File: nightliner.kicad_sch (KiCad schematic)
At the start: 76 parts, among them J1 TYPE-C-31-M-12, SW1 SW_SPST, SW10 SW_SPST, SW11 SW_SPST, SW12 SW_SPST, SW13 SW_SPST, SW14 SW_SPST, SW15 SW_SPST, SW16 SW_SPST, SW17 SW_SPST, SW18 SW_SPST, SW19 SW_SPST, SW2 SW_SPST, SW20 SW_SPST, SW21 ON_OFF, SW22 Reset, SW3 SW_SPST, SW4 SW_SPST, SW5 SW_SPST, SW6 SW_SPST, SW7 SW_SPST, SW8 SW_SPST, SW9 SW_SPST, U1 holyiot-18010, U2 TVS2200DRV, U3 USBLC6-2SC6, U4 BQ24075RGT, U5 XC6220B331MR

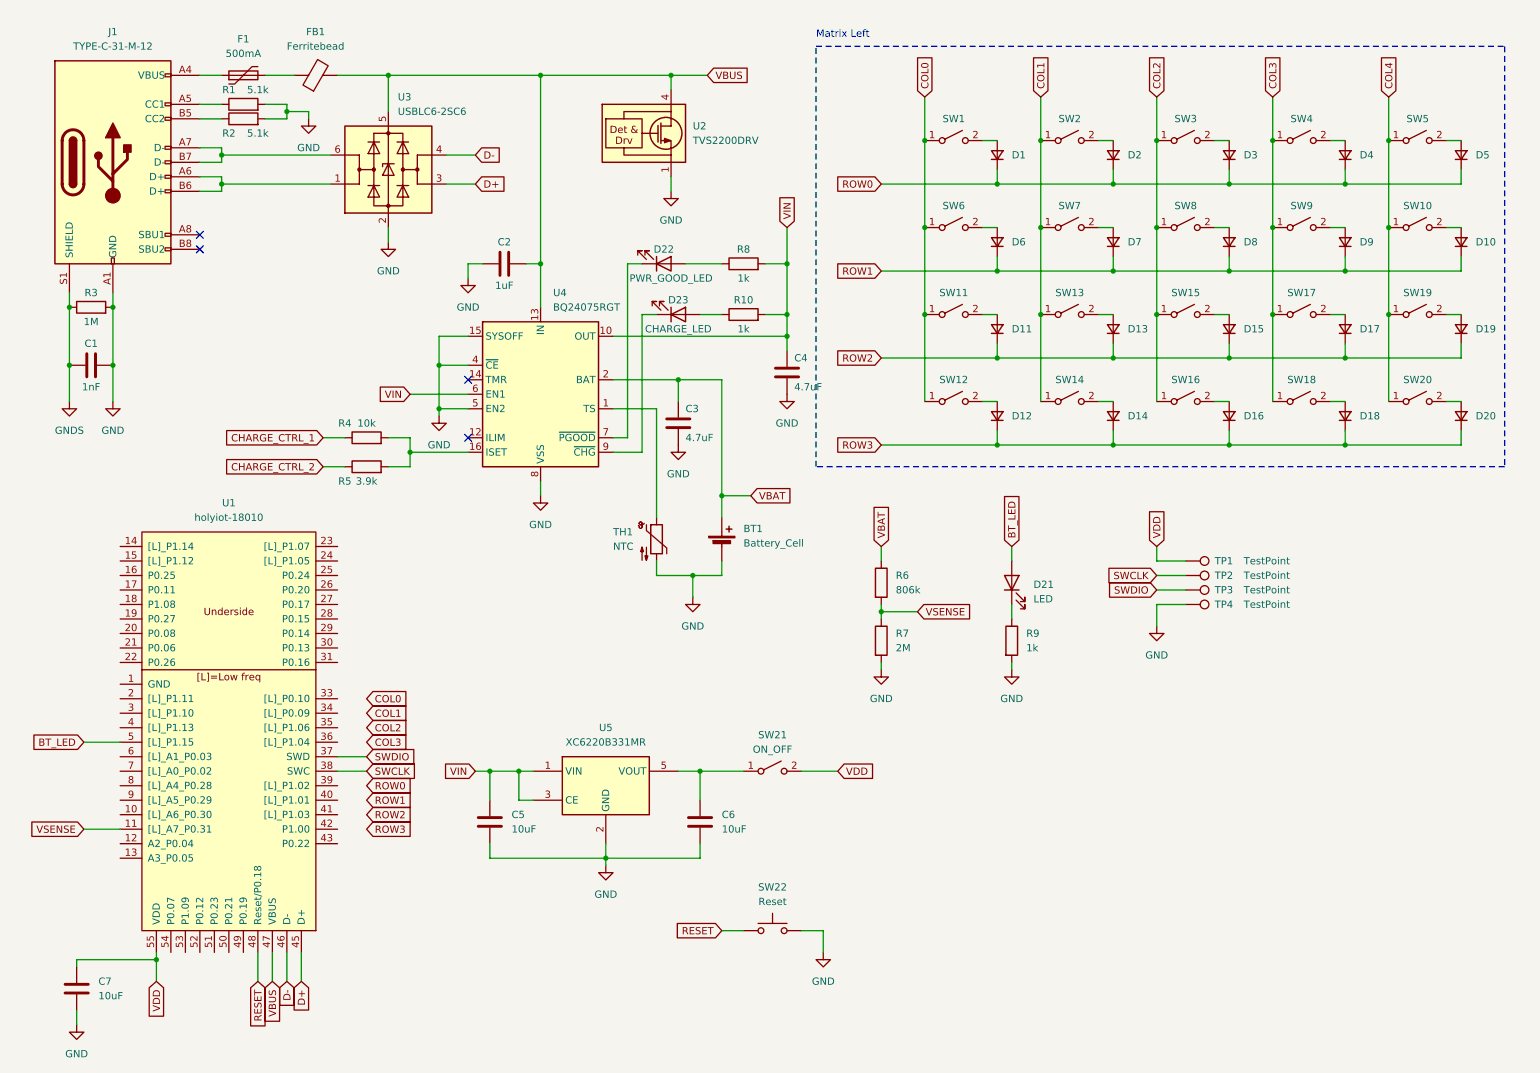
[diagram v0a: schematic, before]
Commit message: feat: schematics with partial footprints
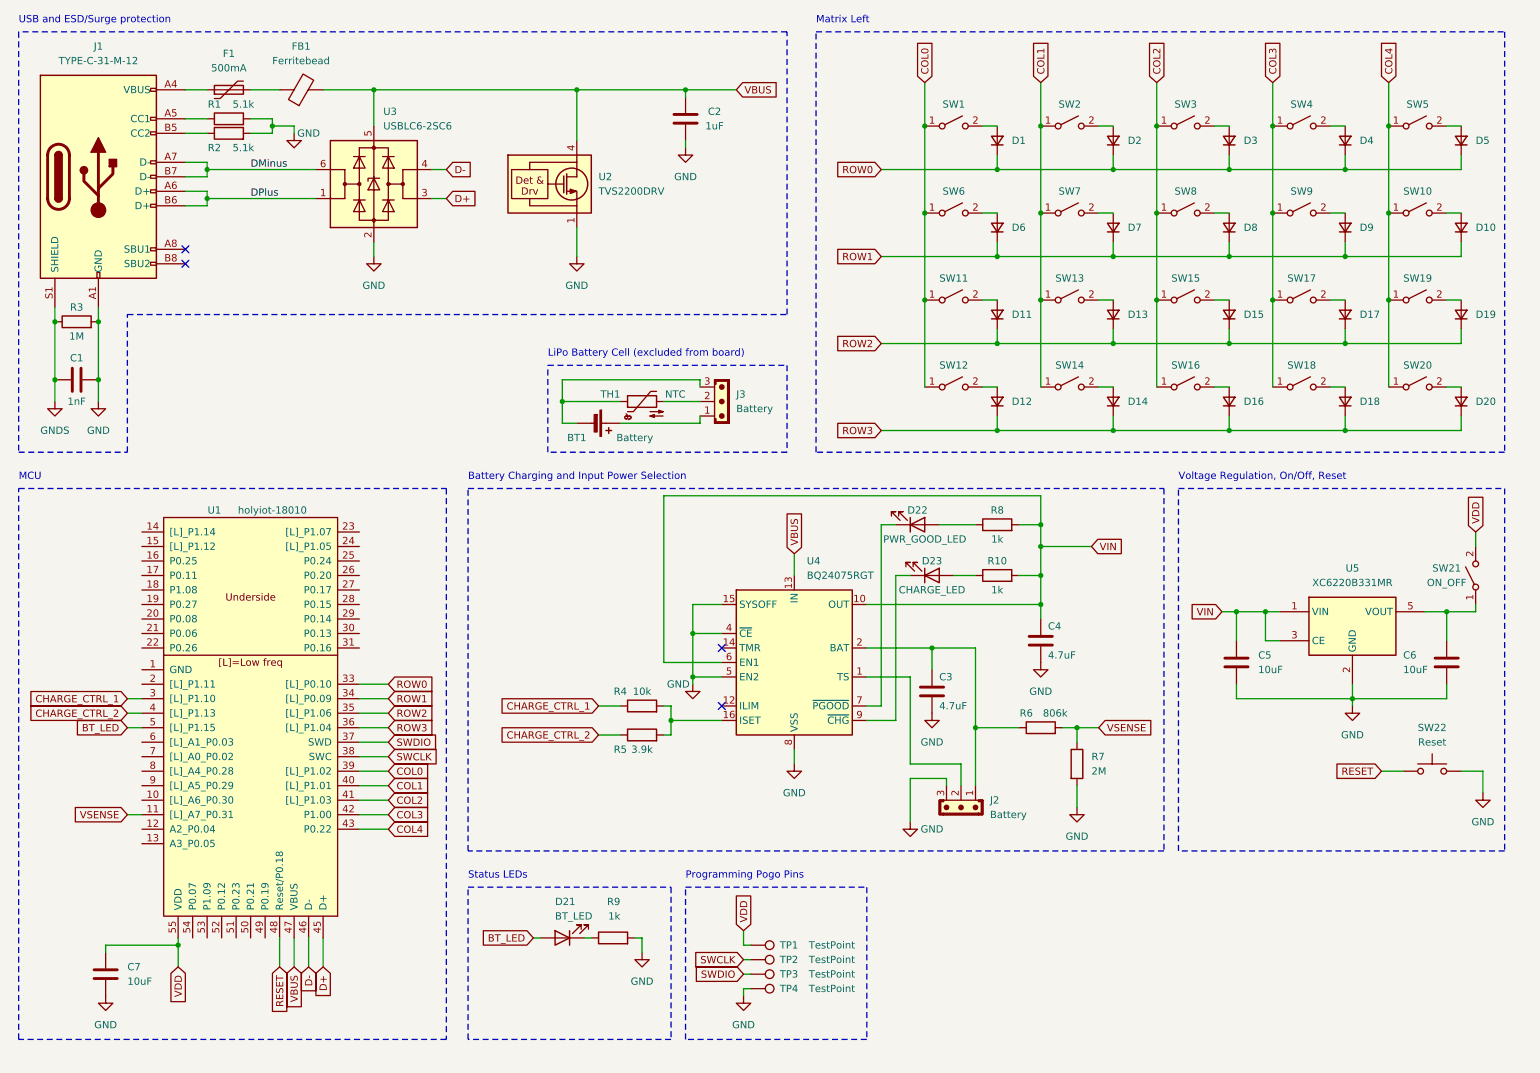
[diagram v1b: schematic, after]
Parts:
- added J2, J3: Battery, Connector_JST:JST_EH_B3B-EH-A_1x03_P2.50mm_Vertical, symbol PCM_SL_Connectors:JST_03
- BT1: value Battery_Cell -> Battery
- D1, D10, D11, D12, D13, D14, D15, D16, D17, D18, D19, D2, D20, D3, D4, D5, D6, D7, D8, D9: footprint (none) -> keebio:D_SOD-323
- D21: value LED -> BT_LED
- SW1, SW10, SW11, SW12, SW13, SW14, SW15, SW16, SW17, SW18, SW19, SW2, SW20, SW3, SW4, SW5, SW6, SW7, SW8, SW9: footprint (none) -> kleeb_choc:pg1350-H
- SW21: footprint (none) -> Button_Switch_SMD:SW_SPDT_PCM12
- TP1, TP2, TP3, TP4: footprint (none) -> TestPoint:TestPoint_Pad_D1.5mm
- U1: footprint mcu:holyiot-18010 -> kleeb_mcu:holyiot-18010
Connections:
- net CHARGE_CTRL_1: now also U1.3 ([L]_P1.10)
- net CHARGE_CTRL_2: now also U1.4 ([L]_P1.13)
- net COL0: now also U1.39 ([L]_P1.02)
- net COL1: now also U1.40 ([L]_P1.01)
- net COL2: now also U1.41 ([L]_P1.03)
- net COL3: now also U1.42 (P1.00)
- net COL4: now also U1.43 (P0.22)
- net GND: now also J2.3; no longer BT1.2 (-), TH1.2
- net ROW0: now also U1.33 ([L]_P0.10)
- net ROW1: now also U1.34 ([L]_P0.09)
- net ROW2: now also U1.35 ([L]_P1.06)
- net ROW3: now also U1.36 ([L]_P1.04)
- net DPlus: now reaches J1.A6 (D+), J1.B6 (D+), U3.1 (I/O1)
- net DMinus: now reaches J1.A7 (D-), J1.B7 (D-), U3.6 (I/O1)
- net at U4.1 (TS): now also J2.2; no longer TH1.1
- net VBAT: no longer names the net of C3.1, R6.1, U4.2 (BAT), U4.3 (BAT)
- net VBAT: now also J2.1; no longer BT1.1 (+)
- new net: BT1.1 (+), J3.1
- new net: J3.2, TH1.2
- new net: BT1.2 (-), J3.3, TH1.1
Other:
- note added: "Battery Charging and Input Power Selection"
- note added: "LiPo Battery Cell (excluded from board)"
- note added: "MCU"
- note added: "Programming Pogo Pins"
- note added: "Status LEDs"
- note added: "USB and ESD/Surge protection"
- note added: "Voltage Regulation, On/Off, Reset"
- company: (none) -> https://github.com/michaelrommel/nightliner
- title: (none) -> nightliner - a split wireless keyboard
- moved on the sheet: BT1, C1, C2, C3, C4, C5, C6, C7, D1, D10, D11, D12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

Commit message: feat: first PCB placement
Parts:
- added D24: BAT_STATUS, Capacitor_SMD:C_0603_1608Metric, symbol Device:LED
- added R11: 1k, Resistor_SMD:R_0805_2012Metric, symbol Device:R
- added SW23: BAT_CHECK, miro_keyboard:SW_Push_1P1T_NO_CK_KSC4xxJ, symbol Switch:SW_Push
- added TP5: TestPoint, TestPoint:TestPoint_Pad_D1.5mm, symbol Connector:TestPoint
- C1, C2, C3, C4, C5, C6, C7: footprint (none) -> Capacitor_SMD:C_0805_2012Metric
- D21: footprint (none) -> Capacitor_SMD:C_0603_1608Metric; LCSCNumber (none) -> C575417; PartNumber (none) -> LTST-C194TBKT
- D22: footprint (none) -> Capacitor_SMD:C_0603_1608Metric; LCSCNumber (none) -> C575432; PartNumber (none) -> LTW-C194TS5
- D23: footprint (none) -> Capacitor_SMD:C_0603_1608Metric; LCSCNumber (none) -> C913101; PartNumber (none) -> LTST-C194KRKT
- F1, FB1: footprint (none) -> Capacitor_SMD:C_0603_1608Metric
- J3, TH1: now left out of the parts list
- R1, R10, R2, R3, R4, R5, R6, R7, R8, R9: footprint (none) -> Resistor_SMD:R_0805_2012Metric
- SW22: value Reset -> RESET; footprint (none) -> miro_keyboard:SW_Push_1P1T_NO_CK_KSC4xxJ
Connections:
- net COL0: now also U1.53 (P1.09); no longer U1.39 ([L]_P1.02)
- net COL1: now also U1.52 (P0.12); no longer U1.40 ([L]_P1.01)
- net COL2: now also U1.51 (P0.23); no longer U1.41 ([L]_P1.03)
- net COL3: now also U1.50 (P0.21); no longer U1.42 (P1.00)
- net COL4: now also U1.49 (P0.19); no longer U1.43 (P0.22)
- net GND: now also R11.2, SW23.2, TP5.1; no longer TP4.1
- net VBAT: now reaches C3.1, J2.1, R6.1, U4.2 (BAT), U4.3 (BAT)
- net BAT_TEMP: now reaches J2.2, U4.1 (TS)
- net BAT_CHECK: now reaches U1.12 (A2_P0.04)
- net BAT_CHECK: now also SW23.1
- net BAT_STAT: now reaches U1.13 (A3_P0.05)
- net BAT_STAT: now also D24.2 (A)
- new net: D24.1 (K), R11.1
- new net SWO: TP4.1, U1.42 (P1.00)
- no-connect marks 4 -> 33
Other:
- note added: "(blue)"
- note added: "(green)"
- note added: "(red)"
- note added: "(white)"
- note added: "Matrix"
- note added: "Voltage Regulation, On/Off, Reset, Battery Check"
- note added: "Z, Z: 0mA (off) 0, Z: 100mA Z, 0: 250mA 0, 0: 350mA"
- note removed: "Matrix Left"
- note removed: "Voltage Regulation, On/Off, Reset"
- company: https://github.com/michaelrommel/nightliner -> Layer-7 Technologies
- moved on the sheet: BT1, C1, C2, C3, C4, C5, C6, D1, D10, D11, D12, D13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

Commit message: feat: PCB placement (with wrong choc pos)
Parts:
- removed SW23: BAT_CHECK, miro_keyboard:SW_Push_1P1T_NO_CK_KSC4xxJ, symbol Switch:SW_Push
- FB1: value Ferritebead -> Ferrite
- J2: footprint Connector_JST:JST_EH_B3B-EH-A_1x03_P2.50mm_Vertical -> Connector_JST:JST_EH_S3B-EH_1x03_P2.50mm_Horizontal
- SW21: footprint Button_Switch_SMD:SW_SPDT_PCM12 -> miro_keyboard:SW_XKB_SS-12D11_SPDT_Angled
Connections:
- net BAT_CHECK: no longer names the net of U1.12 (A2_P0.04)
- no-connect marks 33 -> 34
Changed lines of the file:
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@@
   (no_connect (at 39.37 132.08))
   (no_connect (at 39.37 149.86))
+  (no_connect (at 39.37 157.48))
   (no_connect (at 77.47 123.19))
   (no_connect (at 39.37 144.78))
@@
     (stroke (width 0) (type default))
   )
-  (wire (pts (xy 275.59 149.86) (xy 276.86 149.86))
-    (stroke (width 0) (type default))
-  )
   (wire (pts (xy 69.85 33.02) (xy 69.85 34.29))
     (stroke (width 0) (type default))
@@
     (stroke (width 0) (type default))
   )
-  (wire (pts (xy 36.83 157.48) (xy 39.37 157.48))
-    (stroke (width 0) (type default))
-  )
   (wire (pts (xy 252.73 54.61) (xy 252.73 57.15))
     (stroke (width 0) (type default))
@@
     (stroke (width 0) (type default))
   )
-  (wire (pts (xy 276.86 149.86) (xy 276.86 152.4))
-    (stroke (width 0) (type default))
-  )
   (wire (pts (xy 31.75 78.74) (xy 31.75 82.55))
     (stroke (width 0) (type default))
@@
     (stroke (width 0) (type default))
   )
-  (wire (pts (xy 264.16 149.86) (xy 265.43 149.86))
-    (stroke (width 0) (type default))
-  )
   (wire (pts (xy 191.77 57.15) (xy 212.09 57.15))
     (stroke (width 0) (type default))
@@
     )
   )
-  (global_label "BAT_CHECK" (shape input) (at 36.83 157.48 180) (fields_autoplaced)
-    (effects (font (size 1.27 1.27)) (justify right))
-    (property "Intersheetrefs" "${INTERSHEET_REFS}" (at 23.2615 157.48 0)
-      (effects (font (size 1.27 1.27)) (justify right) hide)
-    )
-  )
   (global_label "COL1" (shape input) (at 199.39 26.67 90) (fields_autoplaced)
     (effects (font (size 1.27 1.27)) (justify left))
@@
     )
   )
-  (global_label "BAT_CHECK" (shape input) (at 264.16 149.86 180) (fields_autoplaced)
-    (effects (font (size 1.27 1.27)) (justify right))
-    (property "Intersheetrefs" "${INTERSHEET_REFS}" (at 250.5915 149.86 0)
-      (effects (font (size 1.27 1.27)) (justify right) hide)
-    )
-  )
   (global_label "COL3" (shape input) (at 58.42 181.61 270) (fields_autoplaced)
     (effects (font (size 1.27 1.27)) (justify right))
@@
       (effects (font (size 1.27 1.27)))
     )
-    (property "Value" "Ferritebead" (at 74.8792 22.86 90)
+    (property "Value" "Ferrite" (at 74.8792 22.86 90)
       (effects (font (size 1.27 1.27)))
     )
@@
     )
   )
-  (symbol (lib_id "power:GND") (at 276.86 152.4 0) (unit 1)
-    (in_bom yes) (on_board yes) (dnp no) (fields_autoplaced)
-    (property "Reference" "#PWR019" (at 276.86 158.75 0)
-      (effects (font (size 1.27 1.27)) hide)
-    )
-    (property "Value" "GND" (at 276.86 157.48 0)
-      (effects (font (size 1.27 1.27)))
-    )
-    (property "Footprint" "" (at 276.86 152.4 0)
-      (effects (font (size 1.27 1.27)) hide)
-    )
-    (property "Datasheet" "" (at 276.86 152.4 0)
-      (effects (font (size 1.27 1.27)) hide)
-    )
-    (pin "1")
-    (instances
-      (project "nightliner"
-        (path "/e4693d91-d111-4059-a601-28406aaad775"
-          (reference "#PWR019") (unit 1)
-        )
-      )
-    )
-  )
   (symbol (lib_id "Device:D_Small") (at 252.73 52.07 90) (unit 1)
     (in_bom yes) (on_board yes) (dnp no) (fields_autoplaced)
@@
       (effects (font (size 1.27 1.27)))
     )
-    (property "Footprint" "Button_Switch_SMD:SW_SPDT_PCM12" (at 275.59 113.03 0)
+    (property "Footprint" "miro_keyboard:SW_XKB_SS-12D11_SPDT_Angled" (at 275.59 113.03 0)
       (effects (font (size 1.27 1.27)) hide)
     )
@@
       (effects (font (size 1.27 1.27)) (justify left))
     )
-    (property "Footprint" "Connector_JST:JST_EH_B3B-EH-A_1x03_P2.50mm_Vertical" (at 193.04 153.67 0)
+    (property "Footprint" "Connector_JST:JST_EH_S3B-EH_1x03_P2.50mm_Horizontal" (at 193.04 153.67 0)
       (effects (font (size 1.27 1.27)) hide)
     )
@@
       (effects (font (size 1.27 1.27)) hide)
     )
+    (property "PartNumber" "" (at 185.42 153.67 0)
+      (effects (font (size 1.27 1.27)) hide)
+    )
+    (property "LCSCNumber" "" (at 185.42 153.67 0)
+      (effects (font (size 1.27 1.27)) hide)
+    )
     (pin "1")
     (pin "2")
@@
         )
       )
-    )
-  )
-  (symbol (lib_id "Switch:SW_Push") (at 270.51 149.86 0) (unit 1)
-    (in_bom yes) (on_board yes) (dnp no) (fields_autoplaced)
-    (property "Reference" "SW23" (at 270.51 142.24 0)
-      (effects (font (size 1.27 1.27)))
-    )
-    (property "Value" "BAT_CHECK" (at 270.51 144.78 0)
-      (effects (font (size 1.27 1.27)))
-    )
-    (property "Footprint" "miro_keyboard:SW_Push_1P1T_NO_CK_KSC4xxJ" (at 270.51 144.78 0)
-      (effects (font (size 1.27 1.27)) hide)
-    )
-    (property "Datasheet" "~" (at 270.51 144.78 0)
-      (effects (font (size 1.27 1.27)) hide)
-    )
-    (pin "1")
-    (pin "2")
-    (instances
-      (project "nightliner"
-        (path "/e4693d91-d111-4059-a601-28406aaad775"
-          (reference "SW23") (unit 1)
-        )
-      )
